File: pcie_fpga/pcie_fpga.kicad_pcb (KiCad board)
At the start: 4 copper layers, 167.7 x 68.9 mm, 4 parts, among them J2 PCIexpress_x4, U1 XC7A50T-FGG484, X1 ECS-2520MVQ-1000-BN-TR

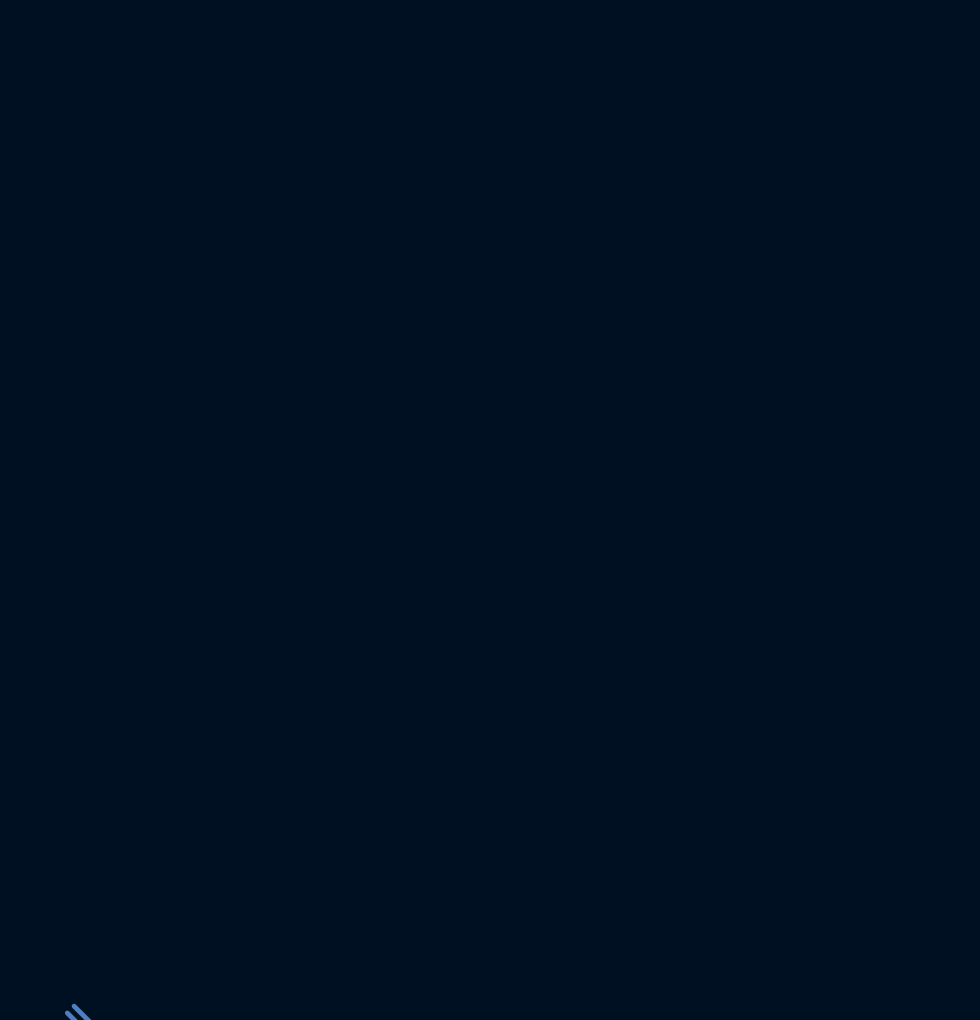
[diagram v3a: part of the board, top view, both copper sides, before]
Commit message: looking at Xilinx Artix Ultrascale+ for pcie board
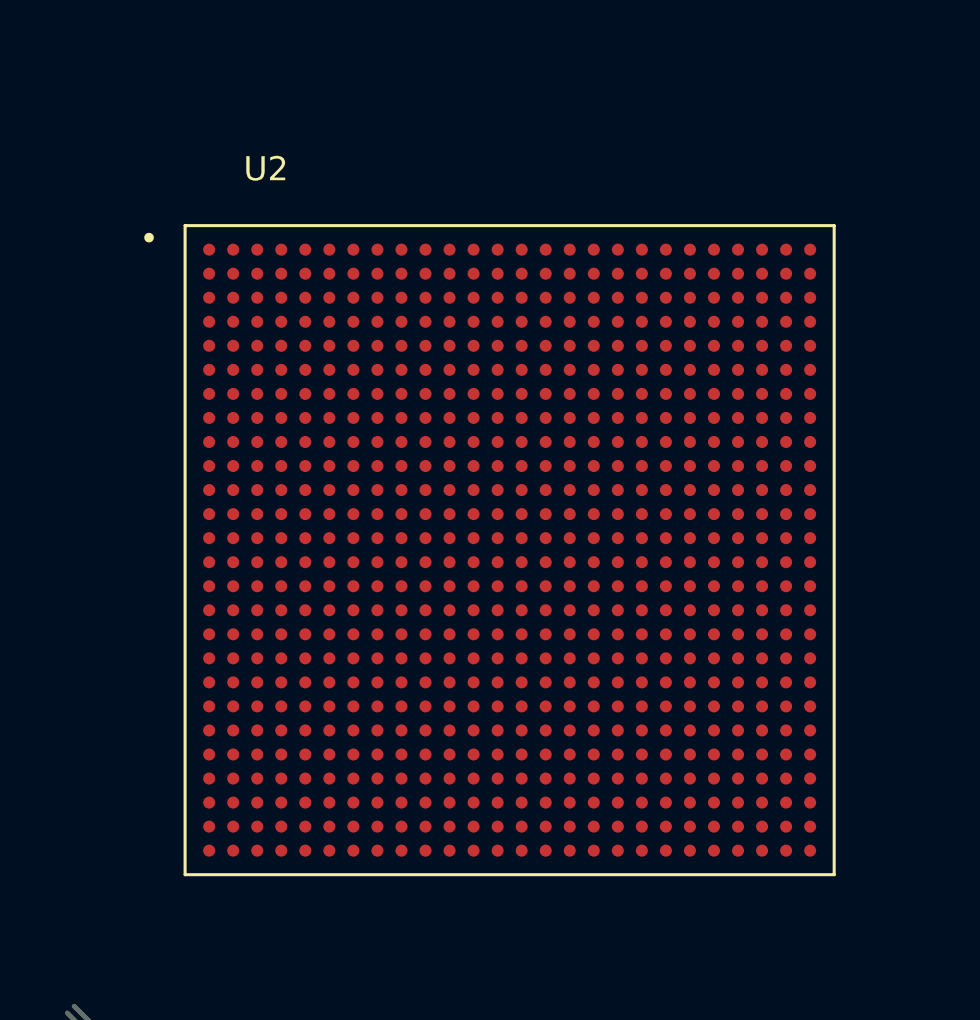
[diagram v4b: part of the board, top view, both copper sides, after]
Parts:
- added U2: XCAU10P-1FFVB676I, pedrolib:IC_XCAU10P-1FFVB676I, F.Cu at (157.7, 156.5)

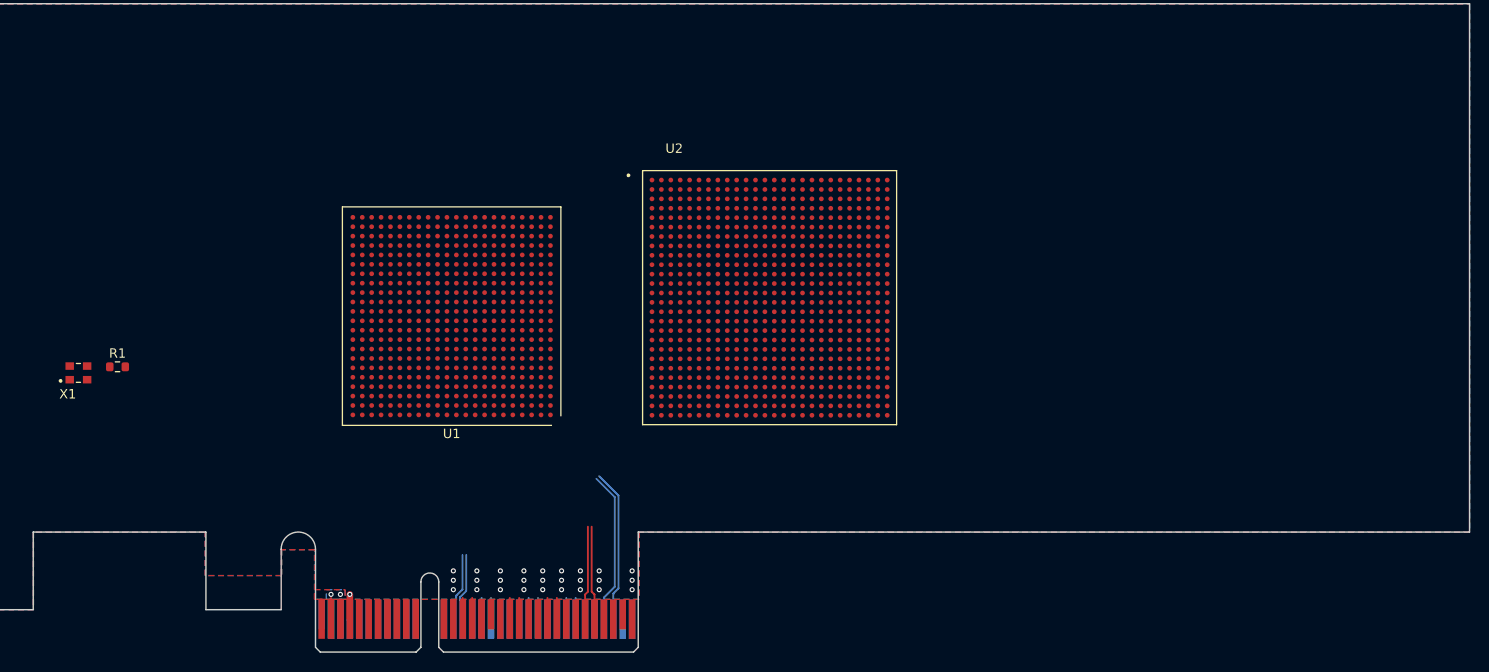
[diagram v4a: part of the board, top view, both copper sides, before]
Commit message: x8 PCIe connector
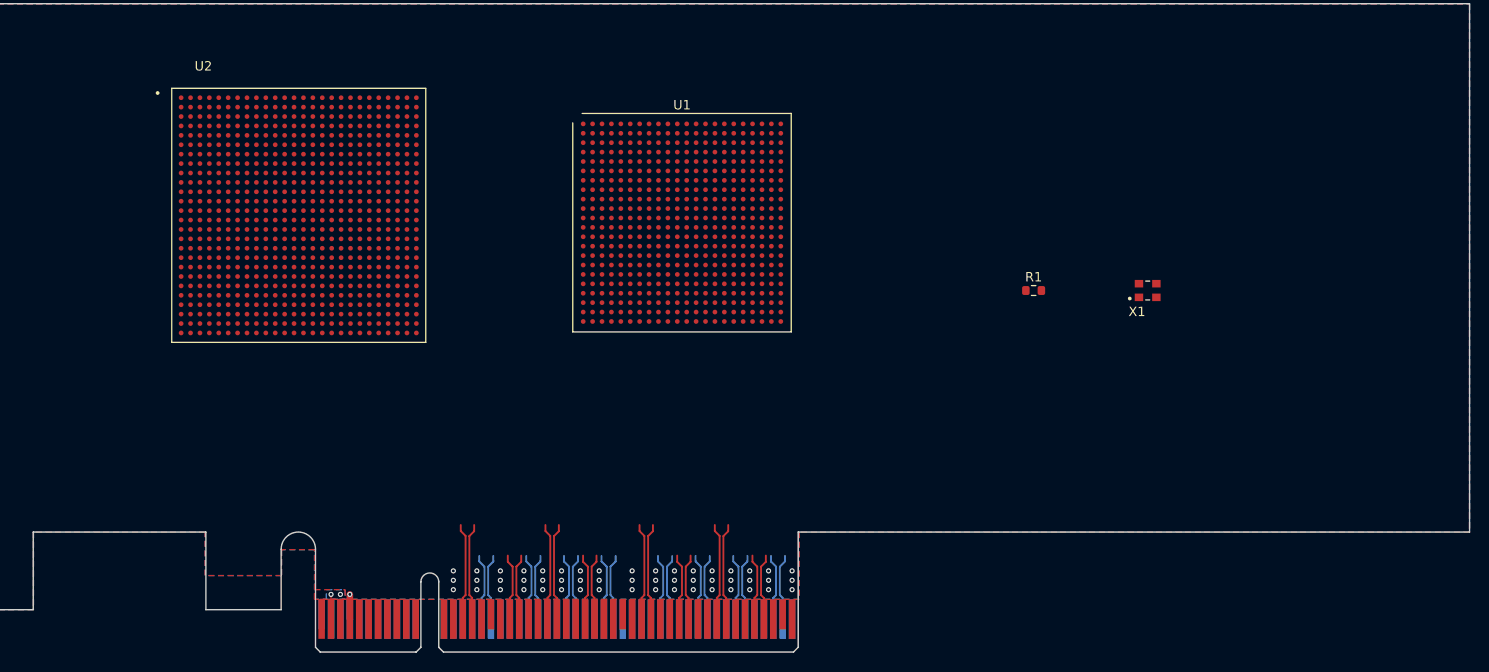
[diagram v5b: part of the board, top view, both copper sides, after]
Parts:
- J2: value PCIexpress_x4 -> PCIexpress_x8; footprint PCIexpress:PCIexpress_x4 -> pedrolib:PCIexpress_x8
- moved X1 114.0 mm to (197.9, 155.7)
- moved R1 97.7 mm to (185.8, 155.7)
- moved U2 50.8 mm to (107.7, 147.7)
- moved U1 26.4 mm to (148.4, 148.5), turned to 0 degrees
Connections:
- J2 pad B31: /prsntn -> unconnected-(J2-PadB31)
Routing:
- net unconnected-(J2-PadB41): track 0.00 -> 10.3 mm
- net unconnected-(J2-PadB33): track 0.00 -> 10.3 mm
- net unconnected-(J2-PadB42): track 0.00 -> 10.3 mm
- net unconnected-(J2-PadB34): track 0.00 -> 10.3 mm
- net /per3_N: track 16.3 -> 7.06 mm
- net /per3_P: track 16.2 -> 7.06 mm
- net /pet2_P: track 2.25 -> 10.3 mm
- net /pet2_N: track 2.25 -> 10.3 mm
- net /pet0_P: track 2.25 -> 10.3 mm
- net /pet0_N: track 2.25 -> 10.3 mm
- net /refclk_P: track 7.21 -> 0.00 mm
- net /refclk_N: track 7.21 -> 0.00 mm
- net unconnected-(J2-PadB46): track 0.00 -> 7.09 mm
- net unconnected-(J2-PadB45): track 0.00 -> 7.09 mm
- net unconnected-(J2-PadB38): track 0.00 -> 7.09 mm
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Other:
- outline, holes or cut-outs redrawn

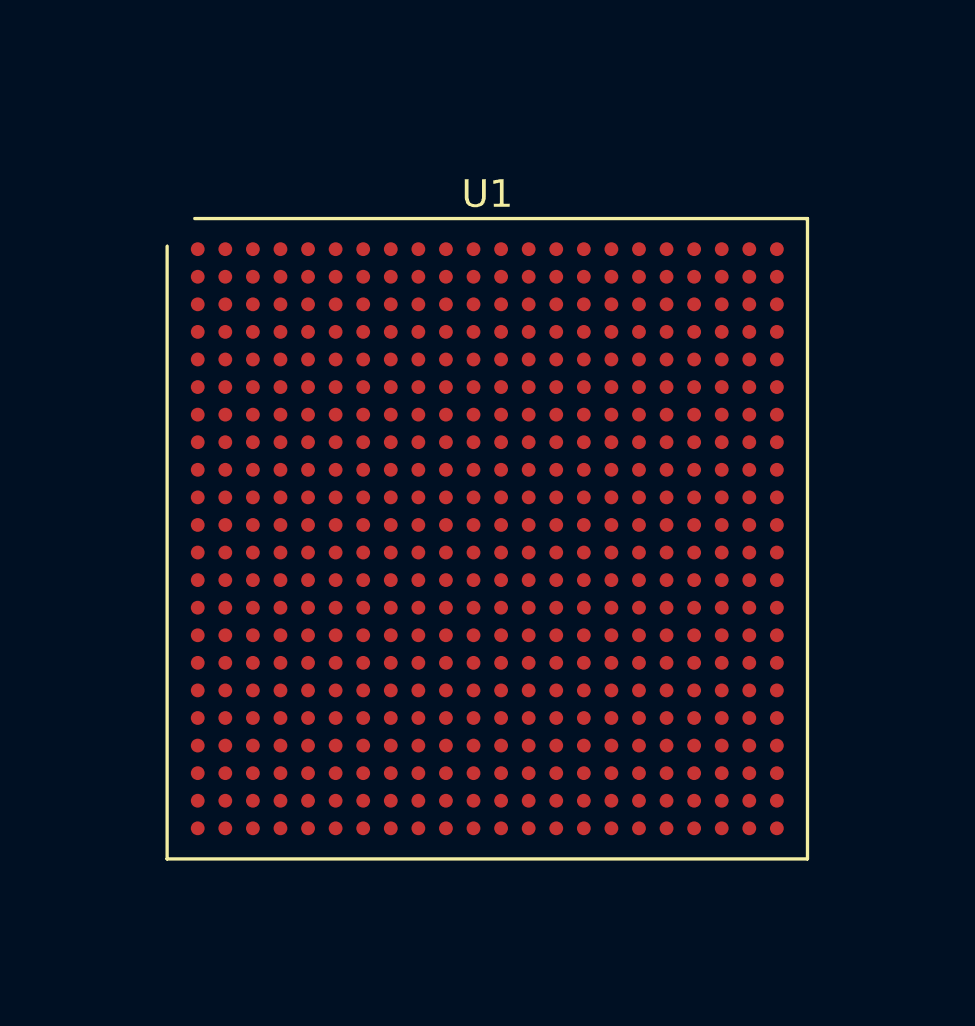
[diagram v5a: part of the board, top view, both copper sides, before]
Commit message: changed out Artix-7 for Artix-UP
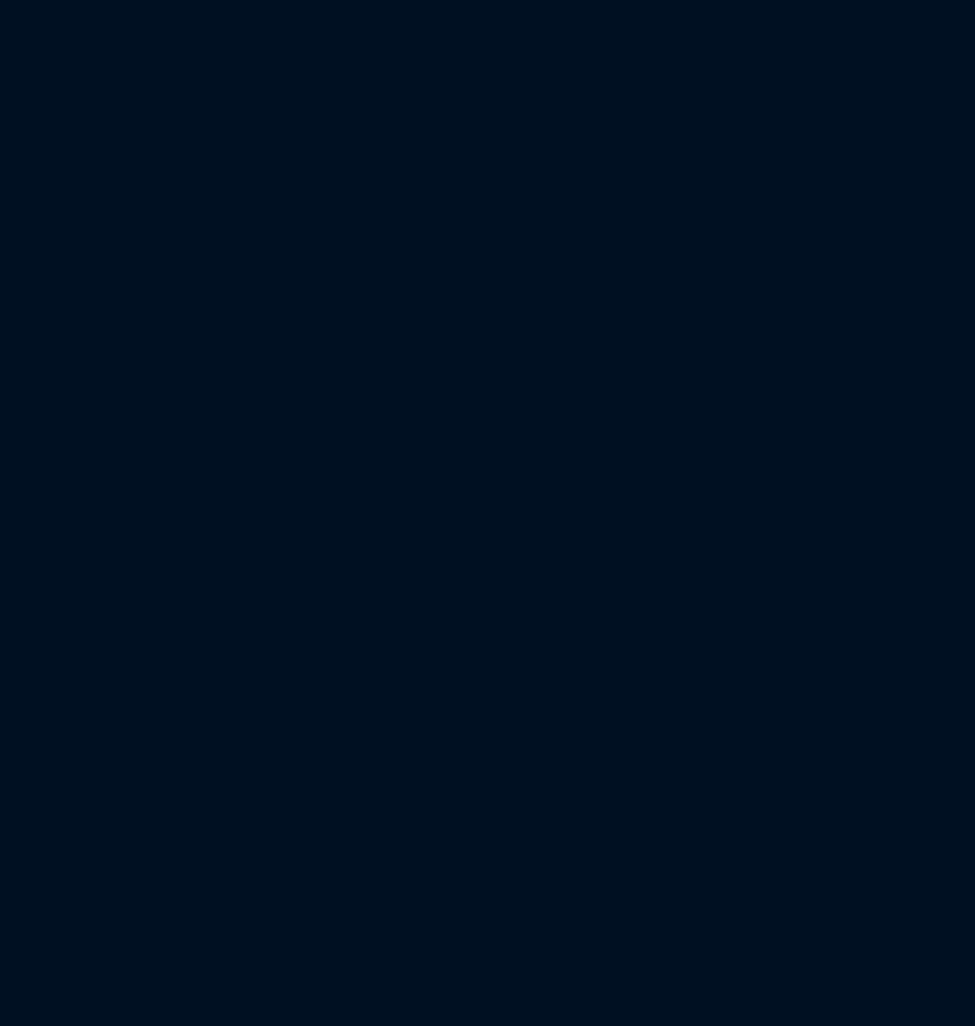
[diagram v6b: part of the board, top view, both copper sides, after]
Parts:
- removed U1: XC7A50T-FGG484, Package_BGA:Xilinx_FGG484
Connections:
- J2 pad A34: unconnected-(J2-PadA34) -> GND
- J2 pad A35: unconnected-(J2-PadA35) -> /per4_P
- J2 pad A36: unconnected-(J2-PadA36) -> /per4_N
- J2 pad A37: unconnected-(J2-PadA37) -> GND
- J2 pad A38: unconnected-(J2-PadA38) -> GND
- J2 pad A39: unconnected-(J2-PadA39) -> /per5_P
- J2 pad A40: unconnected-(J2-PadA40) -> /per5_N
- J2 pad A41: unconnected-(J2-PadA41) -> GND
- J2 pad A42: unconnected-(J2-PadA42) -> GND
- J2 pad A43: unconnected-(J2-PadA43) -> /per6_P
- J2 pad A44: unconnected-(J2-PadA44) -> /per6_N
- J2 pad A45: unconnected-(J2-PadA45) -> GND
- J2 pad A46: unconnected-(J2-PadA46) -> GND
- J2 pad A47: unconnected-(J2-PadA47) -> /per7_P
- J2 pad A48: unconnected-(J2-PadA48) -> /per7_N
- J2 pad A49: unconnected-(J2-PadA49) -> GND
- J2 pad B33: unconnected-(J2-PadB33) -> /pet4_P
- J2 pad B34: unconnected-(J2-PadB34) -> /pet4_N
- J2 pad B35: unconnected-(J2-PadB35) -> GND
- J2 pad B36: unconnected-(J2-PadB36) -> GND
- J2 pad B37: unconnected-(J2-PadB37) -> /pet5_P
- J2 pad B38: unconnected-(J2-PadB38) -> /pet5_N
- J2 pad B39: unconnected-(J2-PadB39) -> GND
- J2 pad B40: unconnected-(J2-PadB40) -> GND
- J2 pad B41: unconnected-(J2-PadB41) -> /pet6_P
- J2 pad B42: unconnected-(J2-PadB42) -> /pet6_N
- J2 pad B43: unconnected-(J2-PadB43) -> GND
- J2 pad B44: unconnected-(J2-PadB44) -> GND
- J2 pad B45: unconnected-(J2-PadB45) -> /pet7_P
- J2 pad B46: unconnected-(J2-PadB46) -> /pet7_N
- J2 pad B47: unconnected-(J2-PadB47) -> GND
- J2 pad B49: unconnected-(J2-PadB49) -> GND
- U2 pad A1: Net-(U2-PadA1) -> GND
- U2 pad A11: Net-(U2-PadA1) -> GND
- U2 pad A16: Net-(U2-PadA1) -> GND
- U2 pad A2: Net-(U2-PadA1) -> GND
- U2 pad A21: Net-(U2-PadA1) -> GND
- U2 pad A26: Net-(U2-PadA1) -> GND
- U2 pad A5: Net-(U2-PadA1) -> GND
- U2 pad A6: Net-(U2-PadA1) -> GND
- U2 pad A8: Net-(U2-PadA1) -> GND
- U2 pad AA1: Net-(U2-PadA1) -> GND
- U2 pad AA16: Net-(U2-PadAA16) -> GND
- U2 pad AA2: Net-(U2-PadA1) -> GND
- U2 pad AA26: Net-(U2-PadAA16) -> GND
- U2 pad AA3: Net-(U2-PadA1) -> GND
- U2 pad AA6: Net-(U2-PadAA16) -> GND
- U2 pad AA8: Net-(U2-PadAA16) -> GND
- U2 pad AB13: Net-(U2-PadAA16) -> GND
- U2 pad AB23: Net-(U2-PadAA16) -> GND
- U2 pad AB3: Net-(U2-PadAA16) -> GND
- U2 pad AB4: Net-(U2-PadAA16) -> GND
- U2 pad AB8: Net-(U2-PadAA16) -> GND
- U2 pad AC1: Net-(U2-PadAA16) -> GND
- U2 pad AC10: Net-(U2-PadAC10) -> GND
- U2 pad AC2: Net-(U2-PadAA16) -> GND
- U2 pad AC20: Net-(U2-PadAC10) -> GND
- U2 pad AC25: Net-(U2-PadAC10) -> GND
- U2 pad AC3: Net-(U2-PadAA16) -> GND
- U2 pad AC6: Net-(U2-PadAC10) -> GND
- U2 pad AC8: Net-(U2-PadAC10) -> GND
- U2 pad AC9: Net-(U2-PadAC10) -> GND
- U2 pad AD10: Net-(U2-PadAC10) -> GND
- U2 pad AD17: Net-(U2-PadAC10) -> GND
- U2 pad AD3: Net-(U2-PadAC10) -> GND
- U2 pad AD4: Net-(U2-PadAC10) -> GND
- U2 pad AD5: Net-(U2-PadAC10) -> GND
- U2 pad AE1: Net-(U2-PadAC10) -> GND
- U2 pad AE10: Net-(U2-PadAE10) -> GND
- U2 pad AE14: Net-(U2-PadAE10) -> GND
- U2 pad AE19: Net-(U2-PadAE10) -> GND
- U2 pad AE2: Net-(U2-PadAE10) -> GND
- U2 pad AE24: Net-(U2-PadAE10) -> GND
- U2 pad AE5: Net-(U2-PadAE10) -> GND
- U2 pad AE6: Net-(U2-PadAE10) -> GND
- U2 pad AF10: Net-(U2-PadAF10) -> GND
- U2 pad AF11: Net-(U2-PadAF10) -> GND
- U2 pad AF16: Net-(U2-PadAF10) -> GND
- U2 pad AF21: Net-(U2-PadAF10) -> GND
- U2 pad AF26: Net-(U2-PadAF10) -> GND
- U2 pad AF3: Net-(U2-PadAE10) -> GND
- U2 pad AF4: Net-(U2-PadAE10) -> GND
- U2 pad AF5: Net-(U2-PadAE10) -> GND
- U2 pad AF8: Net-(U2-PadAE10) -> GND
- U2 pad AF9: Net-(U2-PadAE10) -> GND
- U2 pad B13: Net-(U2-PadAF10) -> GND
- U2 pad B18: Net-(U2-PadAF10) -> GND
- U2 pad B23: Net-(U2-PadAF10) -> GND
- U2 pad B3: Net-(U2-PadAF10) -> GND
- U2 pad B4: Net-(U2-PadAF10) -> GND
- U2 pad B5: Net-(U2-PadAF10) -> GND
- U2 pad B8: Net-(U2-PadAF10) -> GND
- U2 pad C1: Net-(U2-PadC1) -> GND
- U2 pad C10: Net-(U2-PadC1) -> GND
- U2 pad C15: Net-(U2-PadC1) -> GND
- U2 pad C2: Net-(U2-PadC1) -> GND
- U2 pad C25: Net-(U2-PadC1) -> GND
- U2 pad C5: Net-(U2-PadC1) -> GND
- U2 pad C6: Net-(U2-PadC1) -> GND
- U2 pad C8: Net-(U2-PadC1) -> GND
- U2 pad D12: Net-(U2-PadD12) -> GND
- U2 pad D22: Net-(U2-PadD12) -> GND
- U2 pad D3: Net-(U2-PadC1) -> GND
- U2 pad D4: Net-(U2-PadC1) -> GND
- U2 pad D5: Net-(U2-PadC1) -> GND
- U2 pad D8: Net-(U2-PadC1) -> GND
- U2 pad E1: Net-(U2-PadD12) -> GND
- U2 pad E19: Net-(U2-PadD12) -> GND
- U2 pad E2: Net-(U2-PadD12) -> GND
- U2 pad E3: Net-(U2-PadD12) -> GND
- U2 pad E6: Net-(U2-PadD12) -> GND
- U2 pad E8: Net-(U2-PadD12) -> GND
- U2 pad F11: Net-(U2-PadD12) -> GND
- U2 pad F16: Net-(U2-PadF16) -> GND
- U2 pad F21: Net-(U2-PadF16) -> GND
- U2 pad F26: Net-(U2-PadF16) -> GND
- U2 pad F3: Net-(U2-PadD12) -> GND
- U2 pad F4: Net-(U2-PadD12) -> GND
- U2 pad F8: Net-(U2-PadD12) -> GND
- U2 pad G1: Net-(U2-PadF16) -> GND
- U2 pad G13: Net-(U2-PadF16) -> GND
- U2 pad G2: Net-(U2-PadF16) -> GND
- U2 pad G23: Net-(U2-PadF16) -> GND
- U2 pad G3: Net-(U2-PadF16) -> GND
- U2 pad G6: Net-(U2-PadF16) -> GND
- U2 pad G8: Net-(U2-PadF16) -> GND
- U2 pad H20: Net-(U2-PadH20) -> GND
- U2 pad H3: Net-(U2-PadF16) -> GND
- U2 pad H4: Net-(U2-PadF16) -> GND
- U2 pad H8: Net-(U2-PadH20) -> GND
- U2 pad J1: Net-(U2-PadH20) -> GND
- U2 pad J17: Net-(U2-PadH20) -> GND
- U2 pad J2: Net-(U2-PadH20) -> GND
- U2 pad J3: Net-(U2-PadH20) -> GND
- U2 pad J6: Net-(U2-PadH20) -> GND
- U2 pad J8: Net-(U2-PadH20) -> GND
- U2 pad K12: Net-(U2-PadH20) -> GND
- U2 pad K14: Net-(U2-PadK14) -> GND
- U2 pad K16: Net-(U2-PadK14) -> GND
- U2 pad K19: Net-(U2-PadK14) -> GND
- U2 pad K24: Net-(U2-PadK14) -> GND
- U2 pad K3: Net-(U2-PadH20) -> GND
- U2 pad K4: Net-(U2-PadH20) -> GND
- U2 pad K8: Net-(U2-PadH20) -> GND
- U2 pad L1: Net-(U2-PadK14) -> GND
- U2 pad L11: Net-(U2-PadK14) -> GND
- U2 pad L13: Net-(U2-PadK14) -> GND
- U2 pad L15: Net-(U2-PadK14) -> GND
- U2 pad L17: Net-(U2-PadL17) -> GND
- U2 pad L2: Net-(U2-PadK14) -> GND
- U2 pad L21: Net-(U2-PadL17) -> GND
- U2 pad L26: Net-(U2-PadL17) -> GND
- U2 pad L3: Net-(U2-PadK14) -> GND
- U2 pad L6: Net-(U2-PadK14) -> GND
- U2 pad L8: Net-(U2-PadK14) -> GND
- U2 pad M10: Net-(U2-PadL17) -> GND
- U2 pad M12: Net-(U2-PadL17) -> GND
- U2 pad M14: Net-(U2-PadL17) -> GND
- U2 pad M16: Net-(U2-PadL17) -> GND
- U2 pad M23: Net-(U2-PadL17) -> GND
- U2 pad M3: Net-(U2-PadL17) -> GND
- U2 pad M4: Net-(U2-PadL17) -> GND
- U2 pad M8: Net-(U2-PadL17) -> GND
- U2 pad N1: Net-(U2-PadL17) -> GND
- U2 pad N11: Net-(U2-PadN11) -> GND
- U2 pad N15: Net-(U2-PadN11) -> GND
- U2 pad N17: Net-(U2-PadN11) -> GND
- U2 pad N2: Net-(U2-PadN11) -> GND
- U2 pad N20: Net-(U2-PadN11) -> GND
- U2 pad N25: Net-(U2-PadN11) -> GND
- U2 pad N3: Net-(U2-PadN11) -> GND
- U2 pad N6: Net-(U2-PadN11) -> GND
- U2 pad N8: Net-(U2-PadN11) -> GND
- U2 pad P10: Net-(U2-PadN11) -> GND
- U2 pad P12: Net-(U2-PadP12) -> GND
- U2 pad P16: Net-(U2-PadP12) -> GND
- U2 pad P3: Net-(U2-PadN11) -> GND
- U2 pad P4: Net-(U2-PadN11) -> GND
- U2 pad P8: Net-(U2-PadN11) -> GND
- U2 pad R1: Net-(U2-PadP12) -> GND
- U2 pad R11: Net-(U2-PadP12) -> GND
- U2 pad R15: Net-(U2-PadP12) -> GND
- U2 pad R17: Net-(U2-PadP12) -> GND
- U2 pad R19: Net-(U2-PadP12) -> GND
- U2 pad R2: Net-(U2-PadP12) -> GND
- U2 pad R24: Net-(U2-PadP12) -> GND
- U2 pad R3: Net-(U2-PadP12) -> GND
- U2 pad R6: Net-(U2-PadP12) -> GND
- U2 pad R8: Net-(U2-PadP12) -> GND
- U2 pad T10: Net-(U2-PadT10) -> GND
- U2 pad T12: Net-(U2-PadT10) -> GND
- U2 pad T16: Net-(U2-PadT10) -> GND
- U2 pad T21: Net-(U2-PadT10) -> GND
- U2 pad T26: Net-(U2-PadT10) -> GND
- U2 pad T3: Net-(U2-PadT10) -> GND
- U2 pad T4: Net-(U2-PadT10) -> GND
- U2 pad T8: Net-(U2-PadT10) -> GND
- U2 pad U1: Net-(U2-PadT10) -> GND
- U2 pad U11: Net-(U2-PadU11) -> GND
- U2 pad U13: Net-(U2-PadU11) -> GND
- U2 pad U15: Net-(U2-PadU11) -> GND
- U2 pad U17: Net-(U2-PadU11) -> GND
- U2 pad U18: Net-(U2-PadU11) -> GND
- U2 pad U2: Net-(U2-PadT10) -> GND
- U2 pad U3: Net-(U2-PadT10) -> GND
- U2 pad U6: Net-(U2-PadT10) -> GND
- U2 pad U8: Net-(U2-PadU11) -> GND
- U2 pad V10: Net-(U2-PadU11) -> GND
- U2 pad V12: Net-(U2-PadU11) -> GND
- U2 pad V14: Net-(U2-PadU11) -> GND
- U2 pad V16: Net-(U2-PadV16) -> GND
- U2 pad V20: Net-(U2-PadV16) -> GND
- U2 pad V25: Net-(U2-PadV16) -> GND
- U2 pad V3: Net-(U2-PadU11) -> GND
- U2 pad V4: Net-(U2-PadU11) -> GND
- U2 pad V8: Net-(U2-PadU11) -> GND
- U2 pad W1: Net-(U2-PadV16) -> GND
- U2 pad W17: Net-(U2-PadV16) -> GND
- U2 pad W2: Net-(U2-PadV16) -> GND
- U2 pad W22: Net-(U2-PadV16) -> GND
- U2 pad W3: Net-(U2-PadV16) -> GND
- U2 pad W6: Net-(U2-PadV16) -> GND
- U2 pad W8: Net-(U2-PadV16) -> GND
- U2 pad Y19: Net-(U2-PadV16) -> GND
- U2 pad Y3: Net-(U2-PadV16) -> GND
- U2 pad Y4: Net-(U2-PadV16) -> GND
- U2 pad Y8: Net-(U2-PadV16) -> GND
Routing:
- net unconnected-(J2-PadB41): track 10.3 -> 0.00 mm
- net unconnected-(J2-PadB33): track 10.3 -> 0.00 mm
- net /pet6_P: track 0.00 -> 10.3 mm
- net /pet4_P: track 0.00 -> 10.3 mm
- net unconnected-(J2-PadB42): track 10.3 -> 0.00 mm
- net unconnected-(J2-PadB34): track 10.3 -> 0.00 mm
- net /pet6_N: track 0.00 -> 10.3 mm
- net /pet4_N: track 0.00 -> 10.3 mm
- net unconnected-(J2-PadB46): track 7.09 -> 0.00 mm
- net unconnected-(J2-PadB45): track 7.09 -> 0.00 mm
- net unconnected-(J2-PadB38): track 7.09 -> 0.00 mm
- net unconnected-(J2-PadB37): track 7.09 -> 0.00 mm
- net /pet7_P: track 0.00 -> 7.09 mm
- net /pet7_N: track 0.00 -> 7.09 mm
- net /pet5_P: track 0.00 -> 7.09 mm
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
